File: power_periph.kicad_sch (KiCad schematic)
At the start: 6 parts, among them J6 UART_GPS (DS-009: VCC/TX/RX/G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, J7 UART_ELRS (DS-009: VCC/TX/RX/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, J9 I2C_MAG (DS-009: VCC/SCL/SDA/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

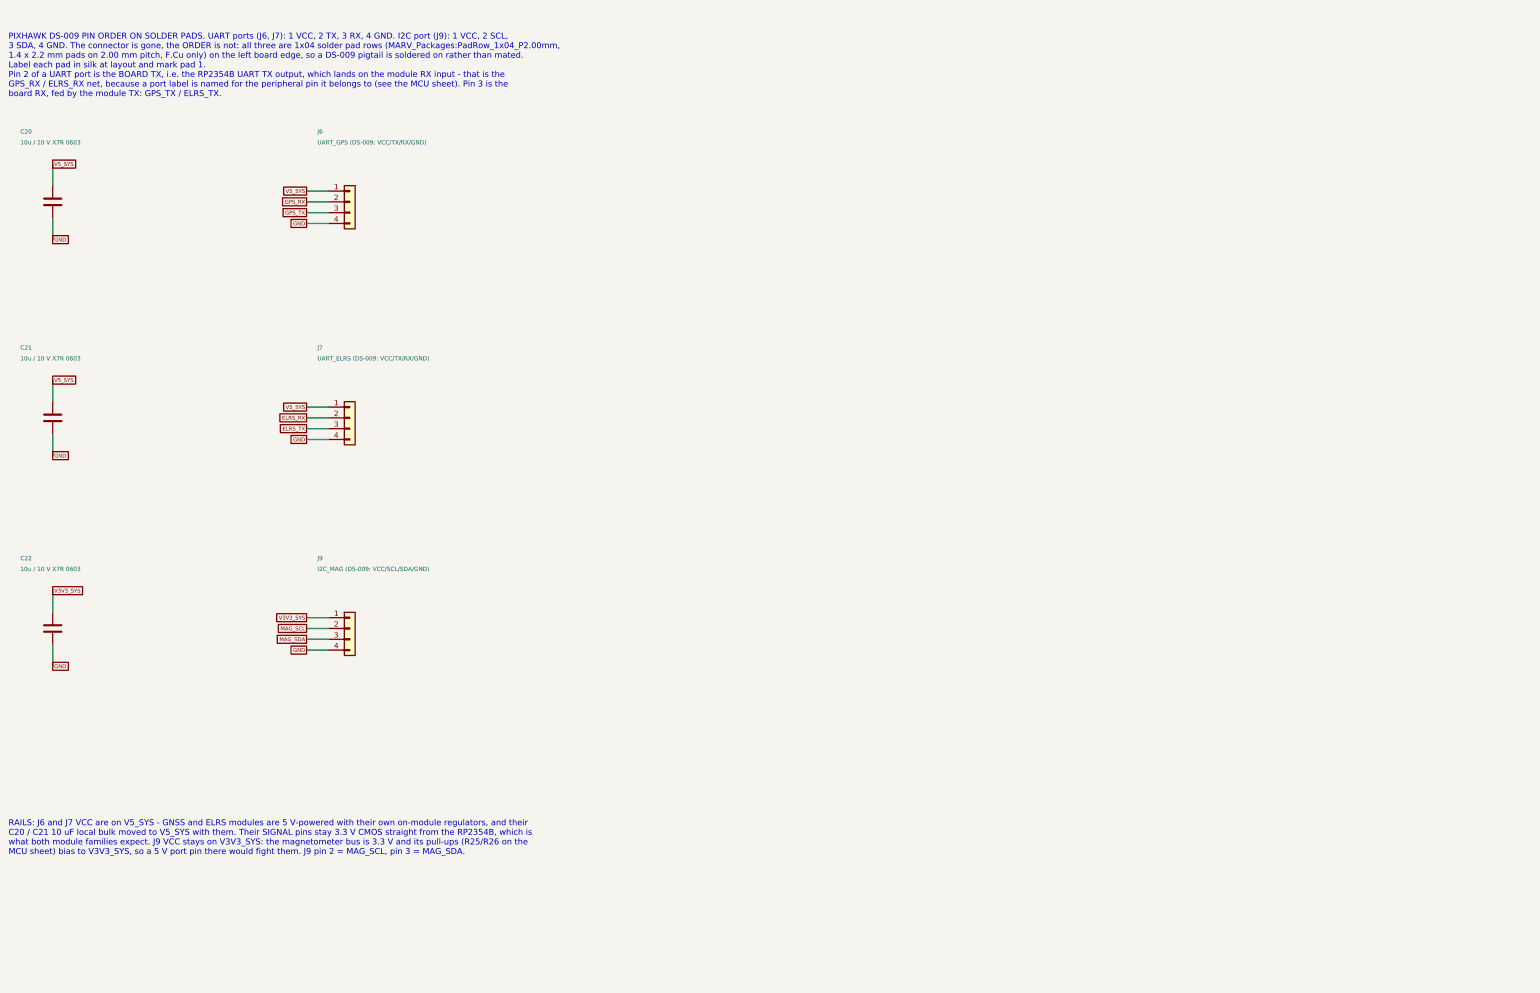
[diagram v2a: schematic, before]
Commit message: IO array replaces bus pad rows; PINOUT.md pin plan; test points; ESC/battery docs
Left edge is now one 2 x 16 through-hole IO array (J6, signal | 5V/3V3/GND
rows, madflight-style) carrying GPS/ELRS/MAG and the ten spare GPIOs; the
J6/J7/J9 pad rows and the J16 block are gone. ESC pad row J3 and DBG pads
J10 stay; servo block J12-J14 stays beside the ESC row. TP1-TP10 1 mm test
points on the sensor SPI, chip selects and interrupts.

PINOUT.md records every GPIO's function and alternates from RP2350
datasheet Table 3, the spare-pin roles (I2C0 on 44/45, SPI1 on 46/47/28,
ADC3-7) and the peripheral ledger; check_power_netlist.py now asserts all
48 GPIO nets against it.

DESIGN_SPEC: ESC connection table, IO array table, test points, battery
monitoring (VBAT_SENSE + ESC current; INA226 rejected), edge allocation.
setup_pcb.py vendors the header footprints with project-local 3D models;
board 50 x 50 mm (48 collides with the grommet keepouts), DRC unrouted-only.
141 components, 105 nets, 231 pin mappings; ERC 0/0, ngspice PASS,
audit 141/141.

Co-Authored-By: Claude Fable 5.1 <noreply@anthropic.com>
Claude-Session: https://claude.ai/code/session_01U6Ud7JA3CDTJZVcZZr5sx1
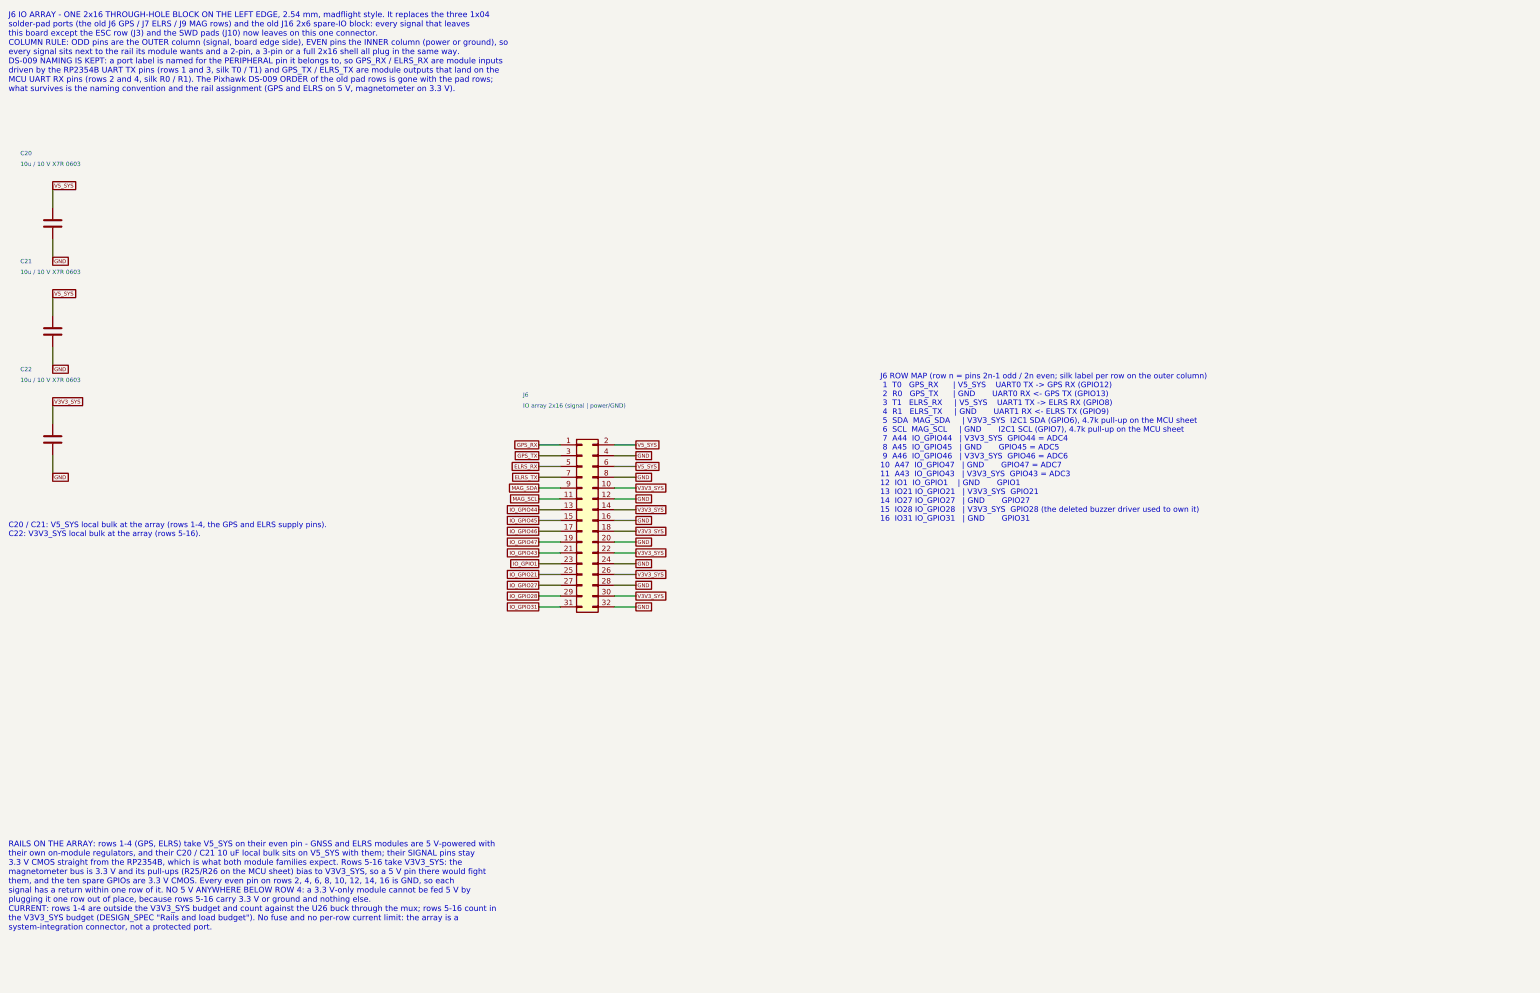
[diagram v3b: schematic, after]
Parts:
- removed J7: UART_ELRS (DS-009: VCC/TX/RX/GND), MARV_Packages:PadRow_1x04_P2.00mm, symbol Connector_Generic:Conn_01x04
- removed J9: I2C_MAG (DS-009: VCC/SCL/SDA/GND), MARV_Packages:PadRow_1x04_P2.00mm, symbol Connector_Generic:Conn_01x04
- J6: value UART_GPS (DS-009: VCC/TX/RX/GND) -> IO array 2x16 (signal | power/GND); footprint MARV_Packages:PadRow_1x04_P2.00mm -> MARV_Packages:PinHeader_2x16_P2.54mm_Vertical_IOArray; symbol Connector_Generic:Conn_01x04 -> Connector_Generic:Conn_02x16_Odd_Even
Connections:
- net ELRS_RX: now also J6.5 (Pin_5)
- net ELRS_TX: now also J6.7 (Pin_7)
- net GND: now also J6.12 (Pin_12), J6.16 (Pin_16), J6.20 (Pin_20), J6.24 (Pin_24), J6.28 (Pin_28), J6.32 (Pin_32), J6.8 (Pin_8)
- net GPS_RX: now also J6.1 (Pin_1); no longer J6.2 (Pin_2)
- net MAG_SCL: now also J6.11 (Pin_11)
- net MAG_SDA: now also J6.9 (Pin_9)
- net V3V3_SYS: now also J6.10 (Pin_10), J6.14 (Pin_14), J6.18 (Pin_18), J6.22 (Pin_22), J6.26 (Pin_26), J6.30 (Pin_30)
- net V5_SYS: now also J6.2 (Pin_2), J6.6 (Pin_6); no longer J6.1 (Pin_1)
- new net IO_GPIO1: J6.23 (Pin_23)
- new net IO_GPIO21: J6.25 (Pin_25)
- new net IO_GPIO27: J6.27 (Pin_27)
- new net IO_GPIO28: J6.29 (Pin_29)
- new net IO_GPIO31: J6.31 (Pin_31)
- new net IO_GPIO43: J6.21 (Pin_21)
- new net IO_GPIO44: J6.13 (Pin_13)
- new net IO_GPIO45: J6.15 (Pin_15)
- new net IO_GPIO46: J6.17 (Pin_17)
- new net IO_GPIO47: J6.19 (Pin_19)
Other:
- note added: "C20 / C21: V5_SYS local bulk at the array (rows 1-4, the GPS and ELRS supply pins). C22: V3V3_SYS local bulk at the array (rows 5-16)."
- note added: "J6 IO ARRAY - ONE 2x16 THROUGH-HOLE BLOCK ON THE LEFT EDGE, 2.54 mm, madflight style. It replaces the three 1x04 solder-pad ports (the old J6 GPS / J7 ELRS / J9 MAG rows) and the old J16 2x6 spare-IO block: every signal that leaves this board except the ESC row (J3) and the SWD pads (J10) now leaves on this one connector. COLUMN RULE: ODD pins are the OUTER column (signal, board edge side), EVEN 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"
- note added: "J6 ROW MAP (row n = pins 2n-1 odd / 2n even; silk label per row on the outer column) 1 T0 GPS_RX | V5_SYS UART0 TX -> GPS RX (GPIO12) 2 R0 GPS_TX | GND UART0 RX <- GPS TX (GPIO13) 3 T1 ELRS_RX | V5_SYS UART1 TX -> ELRS RX (GPIO8) 4 R1 ELRS_TX | GND UART1 RX <- ELRS TX (GPIO9) 5 SDA MAG_SDA | V3V3_SYS I2C1 SDA (GPIO6), 4.7k pull-up on the MCU sheet 6 SCL MAG_SCL | GND I2C1 SCL (GPIO7), 4.7k pull-u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"
- note added: "RAILS ON THE ARRAY: rows 1-4 (GPS, ELRS) take V5_SYS on their even pin - GNSS and ELRS modules are 5 V-powered with their own on-module regulators, and their C20 / C21 10 uF local bulk sits on V5_SYS with them; their SIGNAL pins stay 3.3 V CMOS straight from the RP2354B, which is what both module families expect. Rows 5-16 take V3V3_SYS: the magnetometer bus is 3.3 V and its pull-ups (R25/R26 on 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"
- note removed: "PIXHAWK DS-009 PIN ORDER ON SOLDER PADS. UART ports (J6, J7): 1 VCC, 2 TX, 3 RX, 4 GND. I2C port (J9): 1 VCC, 2 SCL, 3 SDA, 4 GND. The connector is gone, the ORDER is not: all three are 1x04 solder pad rows (MARV_Packages:PadRow_1x04_P2.00mm, 1.4 x 2.2 mm pads on 2.00 mm pitch, F.Cu only) on the left board edge, so a DS-009 pigtail is soldered on rather than mated. Label each pad in silk at layou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"
- note removed: "RAILS: J6 and J7 VCC are on V5_SYS - GNSS and ELRS modules are 5 V-powered with their own on-module regulators, and their C20 / C21 10 uF local bulk moved to V5_SYS with them. Their SIGNAL pins stay 3.3 V CMOS straight from the RP2354B, which is what both module families expect. J9 VCC stays on V3V3_SYS: the magnetometer bus is 3.3 V and its pull-ups (R25/R26 on the MCU sheet) bias to V3V3_SYS, s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"
- title: POWER 3 / peripheral ports -> POWER 3 / IO array
- moved on the sheet: C20, C21, C22

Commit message: Madflight-style layout: 48.7 x 41.2 mm, ESC row left, 3x14 IO block right
Board re-laid out to the madflight FC3v2 arrangement and shrunk from the
50 x 50 square: rectangle 48.7 x 41.2 mm, 30.5 mm mounting square offset
(7.0 mm left margin for the vertical ESC pad row J3, 11.2 mm right margin
for the IO block), grommet keepout Ø6.5. The IO block is three abutting
1x14 rows J6/J7/J8 (signal | 5V/3V3 | GND per row): T0 R0 T1 R1 SDA SCL
S5-S8 A44-A47. The servo block and the 2x16 array are gone (actuators sheet
removed); GPIO 1/21/27/28/31/43 are no-connect (PINOUT.md, checker
updated). microSD ejects off the top edge, USB-C/RESET/BOOT/LED/DBG on the
bottom edge, sensors + test points between the MCU and the IO block.

Courtyard fill 75.7 %, 0 fit/geometry problems, DRC unrouted-only.
140 components; ERC 0/0, checker PASS, ngspice PASS, audit 140/140.
Known: the board-level silk labels on the ESC row and IO block are
mis-nudged by the label fixer (CURR/VBAT/A47 hidden) — silk pass pending.

Co-Authored-By: Claude Fable 5.1 <noreply@anthropic.com>
Claude-Session: https://claude.ai/code/session_01U6Ud7JA3CDTJZVcZZr5sx1
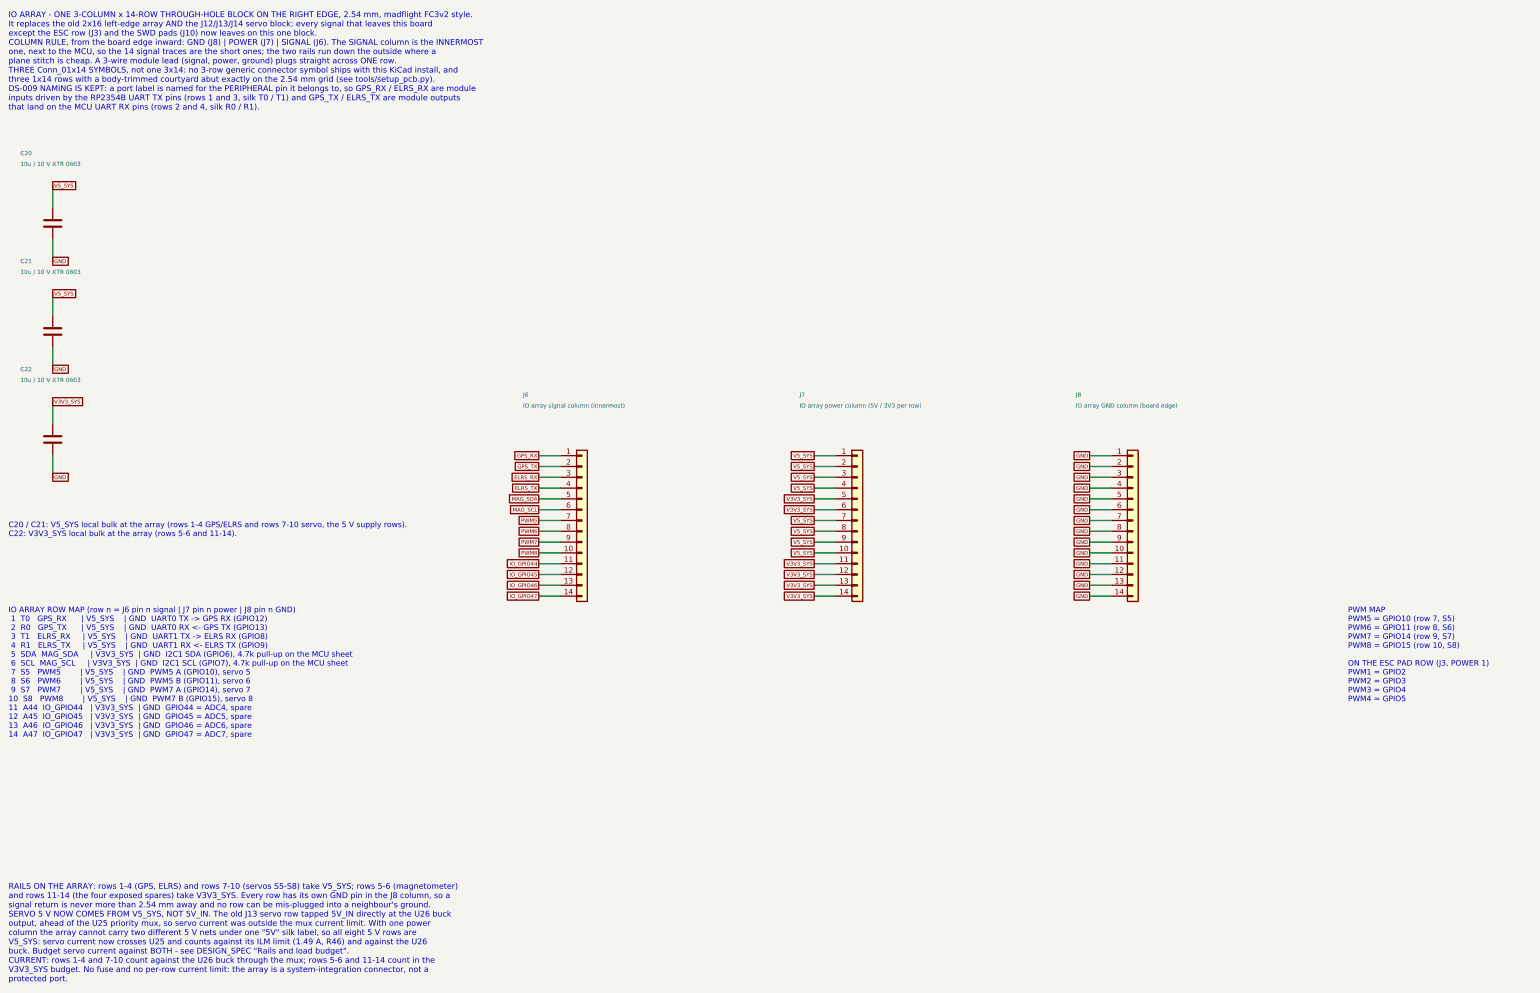
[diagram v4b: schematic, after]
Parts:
- added J7: IO array power column (5V / 3V3 per row), MARV_Packages:PinHeader_1x14_P2.54mm_Vertical_IORow, symbol Connector_Generic:Conn_01x14
- added J8: IO array GND column (board edge), MARV_Packages:PinHeader_1x14_P2.54mm_Vertical_IORow, symbol Connector_Generic:Conn_01x14
- J6: value IO array 2x16 (signal | power/GND) -> IO array signal column (innermost); footprint MARV_Packages:PinHeader_2x16_P2.54mm_Vertical_IOArray -> MARV_Packages:PinHeader_1x14_P2.54mm_Vertical_IORow; symbol Connector_Generic:Conn_02x16_Odd_Even -> Connector_Generic:Conn_01x14
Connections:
- net ELRS_RX: now also J6.3 (Pin_3); no longer J6.5 (Pin_5)
- net ELRS_TX: now also J6.4 (Pin_4); no longer J6.7 (Pin_7)
- net GND: now also J8.1 (Pin_1), J8.10 (Pin_10), J8.11 (Pin_11), J8.12 (Pin_12), J8.13 (Pin_13), J8.14 (Pin_14), J8.2 (Pin_2), J8.3 (Pin_3), J8.4 (Pin_4), J8.5 (Pin_5), J8.6 (Pin_6), J8.7 (Pin_7), J8.8 (Pin_8), J8.9 (Pin_9); no longer J6.12 (Pin_12), J6.16 (Pin_16), J6.20 (Pin_20), J6.24 (Pin_24), J6.28 (Pin_28), J6.32 (Pin_32), J6.4 (Pin_4), J6.8 (Pin_8)
- net GPS_TX: now also J6.2 (Pin_2); no longer J6.3 (Pin_3)
- net IO_GPIO44: now also J6.11 (Pin_11); no longer J6.13 (Pin_13)
- net IO_GPIO45: now also J6.12 (Pin_12); no longer J6.15 (Pin_15)
- net IO_GPIO46: now also J6.13 (Pin_13); no longer J6.17 (Pin_17)
- net IO_GPIO47: now also J6.14 (Pin_14); no longer J6.19 (Pin_19)
- net MAG_SCL: now also J6.6 (Pin_6); no longer J6.11 (Pin_11)
- net MAG_SDA: now also J6.5 (Pin_5); no longer J6.9 (Pin_9)
- net V3V3_SYS: now also J7.11 (Pin_11), J7.12 (Pin_12), J7.13 (Pin_13), J7.14 (Pin_14), J7.5 (Pin_5), J7.6 (Pin_6); no longer J6.10 (Pin_10), J6.14 (Pin_14), J6.18 (Pin_18), J6.22 (Pin_22), J6.26 (Pin_26), J6.30 (Pin_30)
- net V5_SYS: now also J7.1 (Pin_1), J7.10 (Pin_10), J7.2 (Pin_2), J7.3 (Pin_3), J7.4 (Pin_4), J7.7 (Pin_7), J7.8 (Pin_8), J7.9 (Pin_9); no longer J6.2 (Pin_2), J6.6 (Pin_6)
- removed net IO_GPIO1: J6.23 (Pin_23)
- removed net IO_GPIO21: J6.25 (Pin_25)
- removed net IO_GPIO27: J6.27 (Pin_27)
- removed net IO_GPIO28: J6.29 (Pin_29)
- removed net IO_GPIO31: J6.31 (Pin_31)
- removed net IO_GPIO43: J6.21 (Pin_21)
- new net PWM5: J6.7 (Pin_7)
- new net PWM6: J6.8 (Pin_8)
- new net PWM7: J6.9 (Pin_9)
- new net PWM8: J6.10 (Pin_10)
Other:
- note added: "C20 / C21: V5_SYS local bulk at the array (rows 1-4 GPS/ELRS and rows 7-10 servo, the 5 V supply rows). C22: V3V3_SYS local bulk at the array (rows 5-6 and 11-14)."
- note added: "IO ARRAY - ONE 3-COLUMN x 14-ROW THROUGH-HOLE BLOCK ON THE RIGHT EDGE, 2.54 mm, madflight FC3v2 style. It replaces the old 2x16 left-edge array AND the J12/J13/J14 servo block: every signal that leaves this board except the ESC row (J3) and the SWD pads (J10) now leaves on this one block. COLUMN RULE, from the board edge inward: GND (J8) | POWER (J7) | SIGNAL (J6). The SIGNAL column is the INNERM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"
- note added: "IO ARRAY ROW MAP (row n = J6 pin n signal | J7 pin n power | J8 pin n GND) 1 T0 GPS_RX | V5_SYS | GND UART0 TX -> GPS RX (GPIO12) 2 R0 GPS_TX | V5_SYS | GND UART0 RX <- GPS TX (GPIO13) 3 T1 ELRS_RX | V5_SYS | GND UART1 TX -> ELRS RX (GPIO8) 4 R1 ELRS_TX | V5_SYS | GND UART1 RX <- ELRS TX (GPIO9) 5 SDA MAG_SDA | V3V3_SYS | GND I2C1 SDA (GPIO6), 4.7k pull-up on the MCU sheet 6 SCL MAG_SCL | V3V3_SY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"
- note added: "PWM MAP PWM5 = GPIO10 (row 7, S5) PWM6 = GPIO11 (row 8, S6) PWM7 = GPIO14 (row 9, S7) PWM8 = GPIO15 (row 10, S8) ON THE ESC PAD ROW (J3, POWER 1) PWM1 = GPIO2 PWM2 = GPIO3 PWM3 = GPIO4 PWM4 = GPIO5"
- note added: "RAILS ON THE ARRAY: rows 1-4 (GPS, ELRS) and rows 7-10 (servos S5-S8) take V5_SYS; rows 5-6 (magnetometer) and rows 11-14 (the four exposed spares) take V3V3_SYS. Every row has its own GND pin in the J8 column, so a signal return is never more than 2.54 mm away and no row can be mis-plugged into a neighbour's ground. SERVO 5 V NOW COMES FROM V5_SYS, NOT 5V_IN. The old J13 servo row tapped 5V_IN d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"
- note removed: "C20 / C21: V5_SYS local bulk at the array (rows 1-4, the GPS and ELRS supply pins). C22: V3V3_SYS local bulk at the array (rows 5-16)."
- note removed: "J6 IO ARRAY - ONE 2x16 THROUGH-HOLE BLOCK ON THE LEFT EDGE, 2.54 mm, madflight style. It replaces the three 1x04 solder-pad ports (the old J6 GPS / J7 ELRS / J9 MAG rows) and the old J16 2x6 spare-IO block: every signal that leaves this board except the ESC row (J3) and the SWD pads (J10) now leaves on this one connector. COLUMN RULE: ODD pins are the OUTER column (signal, board edge side), EVEN 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"
- note removed: "J6 ROW MAP (row n = pins 2n-1 odd / 2n even; silk label per row on the outer column) 1 T0 GPS_RX | V5_SYS UART0 TX -> GPS RX (GPIO12) 2 R0 GPS_TX | GND UART0 RX <- GPS TX (GPIO13) 3 T1 ELRS_RX | V5_SYS UART1 TX -> ELRS RX (GPIO8) 4 R1 ELRS_TX | GND UART1 RX <- ELRS TX (GPIO9) 5 SDA MAG_SDA | V3V3_SYS I2C1 SDA (GPIO6), 4.7k pull-up on the MCU sheet 6 SCL MAG_SCL | GND I2C1 SCL (GPIO7), 4.7k pull-u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"
- note removed: "RAILS ON THE ARRAY: rows 1-4 (GPS, ELRS) take V5_SYS on their even pin - GNSS and ELRS modules are 5 V-powered with their own on-module regulators, and their C20 / C21 10 uF local bulk sits on V5_SYS with them; their SIGNAL pins stay 3.3 V CMOS straight from the RP2354B, which is what both module families expect. Rows 5-16 take V3V3_SYS: the magnetometer bus is 3.3 V and its pull-ups (R25/R26 on 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"

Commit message: JLCPCB sourcing: Basic-part refactor, LCSC numbers in the schematic, order files and audit
Parts audited line by line against JLCPCB's live catalogue (tools/jlc/,
reports/jlc-audit.md). Resistors move 0201 -> 0402 (JLC's Basic library has
no 0201 resistor), the U7 FB divider becomes 10k/3.16k 0.1 % (15.8k 0.1 % is
not stocked), Y1 becomes TAXM12M4RFBCCT2T (CL 12 pF) with 18 pF loads, L2/L3
become CJIANG FTC303020D2R2MBCA / FTC404030S4R7MGCA (stocked; Isat 5.5 A /
6.0 A at 30 %, footprints + models vendored from KiCad), the 22 uF/25 V and
10 uF lines move to Basic parts. The U24 default fit is W25Q32JVSNIQ (the
W25Q64JVSSIQ is a 208-mil part and never fitted the 150-mil socket).

Every fitted symbol carries a hidden LCSC property stamped from
tools/jlc/lcsc_map.csv; tools/jlc/export_jlc.py writes reports/jlc-bom.csv
and reports/jlc-cpl.csv (top-side SMT, headers unpopulated, U24 DNP).
Result: 46 unique parts, 16 Basic / 1 Preferred / 29 Extended (was 9/1/35),
extended-fee estimate $87 (was $105), $45.68 per board at 10 (was $52.97 with
L2 unsourced). DESIGN_SPEC gains a Manufacturing (JLCPCB) section with the
quote parameters. Board rebuilt (0 fit/geometry, DRC unrouted-only); ERC
0/0, checker PASS, ngspice PASS, audit 140/140.

Co-Authored-By: Claude Fable 5.1 <noreply@anthropic.com>
Claude-Session: https://claude.ai/code/session_01U6Ud7JA3CDTJZVcZZr5sx1
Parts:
- C20, C21, C22: LCSC (none) -> C96446
- J6, J7, J8: LCSC (none) -> C2905490
